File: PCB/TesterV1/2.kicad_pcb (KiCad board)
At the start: 4 copper layers, 28 x 31.5 mm, 11 parts, among them J2 USB_C_Receptacle_USB2.0_16P, U3 ESP32-WROOM-32E, U4 AMS1117-3.3, U5 CH340C

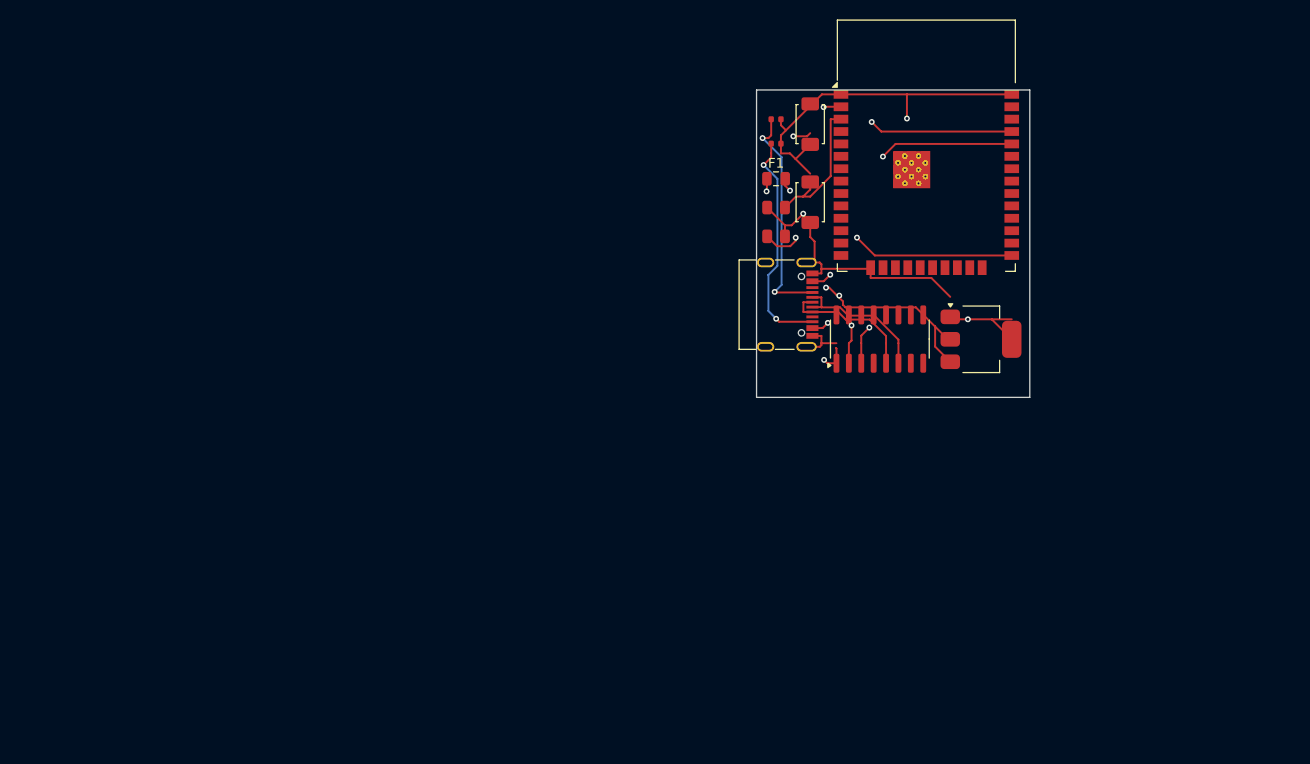
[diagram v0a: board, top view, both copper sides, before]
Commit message: Update PCB footprints, nets and ignore PCB/
Add .gitignore to exclude PCB/ and apply multiple PCB library updates: rename nets (e.g. VCC->BAT, CHRG, STDBY), reassign nets on several pads, and update schematic and fp-info-cache. Replace/update footprints and metadata: convert several resistor footprints from 0402 to 0805 (adjusting values, sizes, pads and 3D models), change fuse footprint to a tactile switch footprint, and update datasheets, LCSC IDs, stock and price fields. Adjust pad geometry, silk/fab text positions/rotations and various UUIDs to match the new footprints and orientation changes.
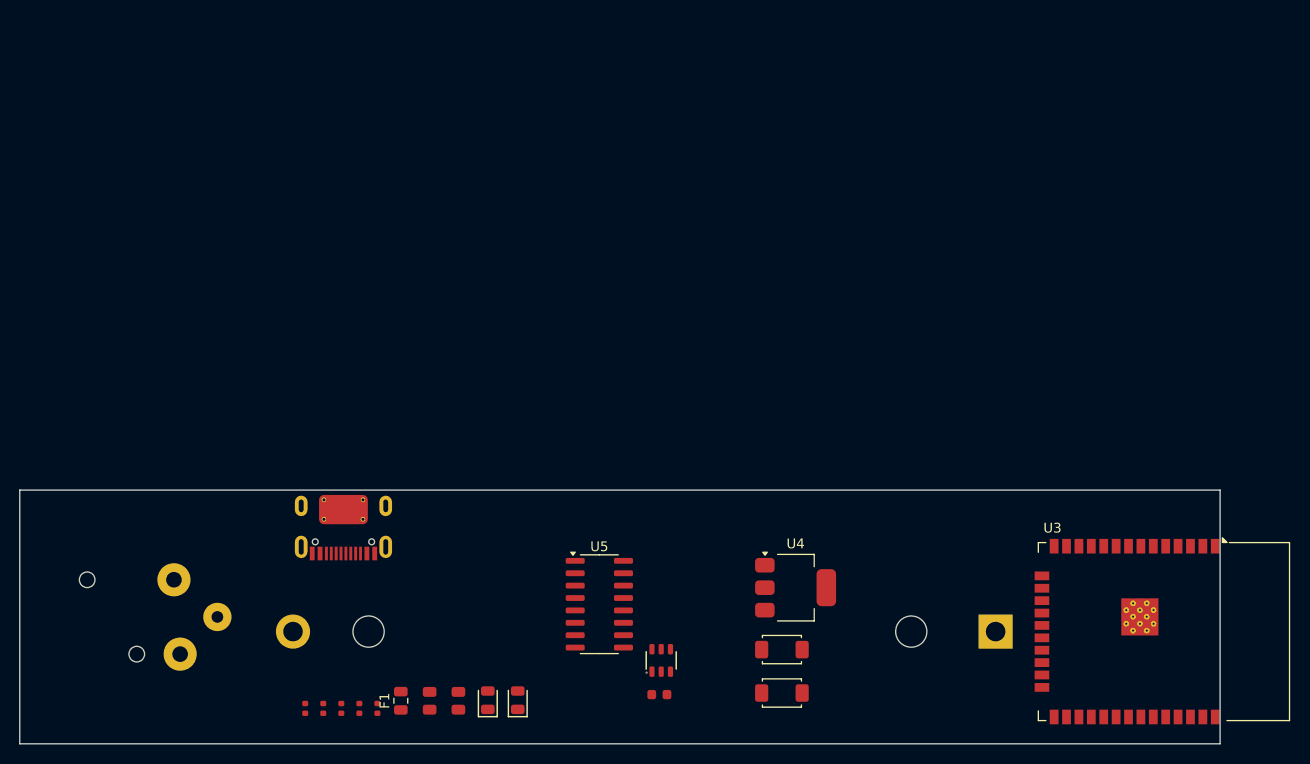
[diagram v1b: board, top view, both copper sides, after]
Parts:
- added BT1: Battery Holder, Battery:BatteryHolder_MPD_BH-18650-PC2, B.Cu at (147.5, 111.0)
- added C1: 10uF, PCM_JLCPCB:C_0603, F.Cu at (113.0, 117.5)
- added D1: Green, PCM_JLCPCB:D_0805, F.Cu at (95.5, 118.0)
- added D2: Red, PCM_JLCPCB:D_0805, F.Cu at (98.5, 118.0)
- added J1: Connector, USB-TYPE-C-16P, PCM_JLCPCB:TYPE-C-SMD_HX-TYPE-C-16PIN, F.Cu at (80.7, 100.5)
- added R3: 1kΩ, PCM_JLCPCB:R_0402, F.Cu at (80.5, 118.9)
- added R4: 1kΩ, PCM_JLCPCB:R_0402, F.Cu at (82.3, 118.9)
- added R7: 1.5kΩ, PCM_JLCPCB:R_0402, F.Cu at (84.2, 118.9)
- added U1: TP4057, PCM_JLCPCB:SOT-23-6_L2.9-W1.6-P0.95-LS2.8-BL, F.Cu at (113.2, 114.0)
- J2: value USB_C_Receptacle_USB2.0_16P -> XLR3; footprint Connector_USB:USB_C_Receptacle_G-Switch_GT-USB-7010ASV -> Connector_Audio:Jack_XLR_Neutrik_NC3FAAH-0_Horizontal; moved to B.Cu
- moved R1 77.3 mm to (76.8, 118.9), turned to 90 degrees
- moved R2 74.2 mm to (78.6, 118.9), turned to 90 degrees
- moved J2 67.8 mm to (63.3, 105.7), turned to 180 degrees
- moved F1 65.9 mm to (86.5, 118.1), turned to 90 degrees
- moved R5 61.8 mm to (89.5, 118.1), turned to 90 degrees
- moved S4 58.4 mm to (125.6, 117.3), turned to 0 degrees
- moved R6 57.7 mm to (92.5, 118.1), turned to 90 degrees
- moved U3 51.4 mm to (161.8, 111.0), turned to -90 degrees
- moved S3 45.9 mm to (125.6, 112.8), turned to 0 degrees
- moved U5 39.6 mm to (106.9, 108.2), turned to 0 degrees
- moved U4 31.8 mm to (127.0, 106.5)
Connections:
- net VCC renamed +5V
- R1 pad 1: Net-(J2-CC1) -> Net-(J1-CC1)
- R2 pad 1: Net-(J2-CC2) -> Net-(J1-CC2)
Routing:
- net GND: track 131.4 -> 0.00 mm, vias 2 -> 0
- net +3V3: track 50.2 -> 0.00 mm, vias 3 -> 0
- net TX: track 40.4 -> 0.00 mm, vias 2 -> 0
- net GPIO0: track 39.2 -> 0.00 mm, vias 3 -> 0
- net RX: track 35.8 -> 0.00 mm, vias 2 -> 0
- net +5V: track 34.1 -> 0.00 mm, vias 3 -> 0
- net Net-(F1-Pad1): track 27.2 -> 0.00 mm, vias 3 -> 0
- net Net-(J2-CC1): track 23.6 -> 0.00 mm, vias 2 -> 0
- net Net-(J2-CC2): track 23.4 -> 0.00 mm, vias 2 -> 0
- net EN: track 14.7 -> 0.00 mm
- net D-: track 14.6 -> 0.00 mm
- net D+: track 14.2 -> 0.00 mm
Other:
- board size 28 x 31.5 mm -> 123 x 26 mm
